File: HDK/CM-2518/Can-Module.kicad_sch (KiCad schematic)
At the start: 13 parts, among them J101 Can Connect, J102 Can Connect, SW101 SW_DIP_x01, U101 SN65HVD230, U102 MCP2515-xST, Y101 8MHz

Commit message: added fd module
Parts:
- removed R102: 10K, Resistor_SMD:R_0402_1005Metric, symbol Device:R
- removed U102: MCP2515-xST, Package_SO:TSSOP-20_4.4x6.5mm_P0.65mm, symbol Interface_CAN_LIN:MCP2515-xST
- added U102: MCP2518FD, Package_SO:SOIC-14_3.9x8.7mm_P1.27mm, symbol Interface_CAN_LIN:MCP2517FD-xSL
- SW101: footprint Button_Switch_SMD:SW_DIP_SPSTx01_Slide_6.7x4.1mm_W6.73mm_P2.54mm_LowProfile_JPin -> Button_Switch_SMD:SW_DIP_SPSTx01_Slide_9.78x4.72mm_W8.61mm_P2.54mm
- Y101: value 8MHz -> 20MHz
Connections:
- net +3V3: now also U102.14 (VDD)
- net CAN_IRQ: now also U102.4 (~{INT})
- net CAN_RX: now also U102.2 (RXCAN)
- net CAN_TX: now also U102.1 (TXCAN)
- net GND: now also U102.7 (VSS)
- net OSC_IN: now also U102.6 (OSC1)
- net OSC_OUT: now also U102.5 (OSC2)
- net SOF: now also U102.3 (CLKO/SOF)
- net SPI_MISO: now also U102.12 (SDO)
- net SPI_MOSI: now also U102.11 (SDI)
- net SPI_SCK: now also U102.10 (SCK)
- net ~{CS}: now also U102.13 (nCS)
- no-connect marks 6 -> 3

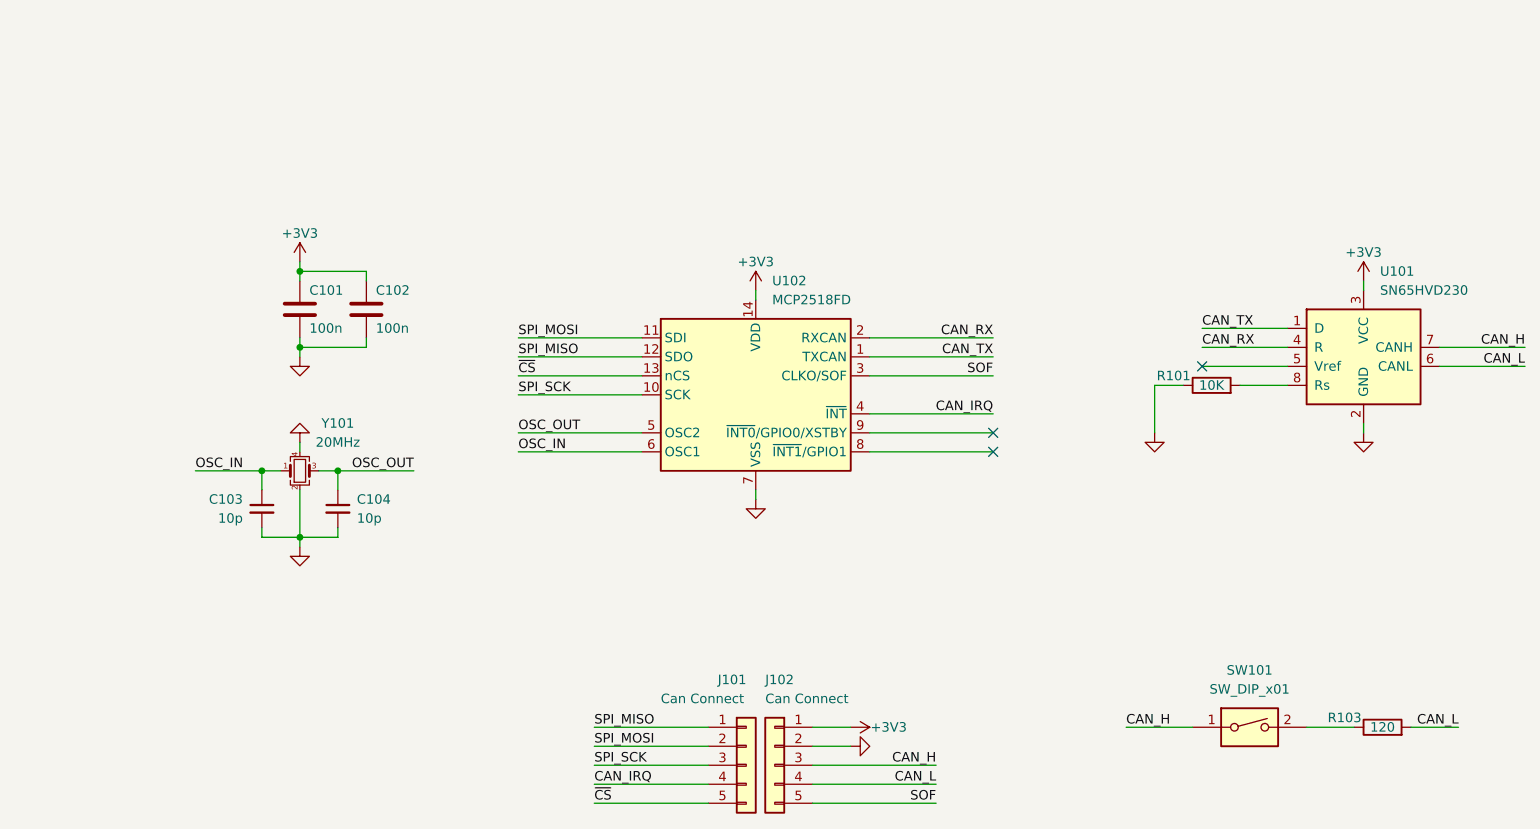
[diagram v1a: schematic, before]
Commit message: updated CM-2518FD Module
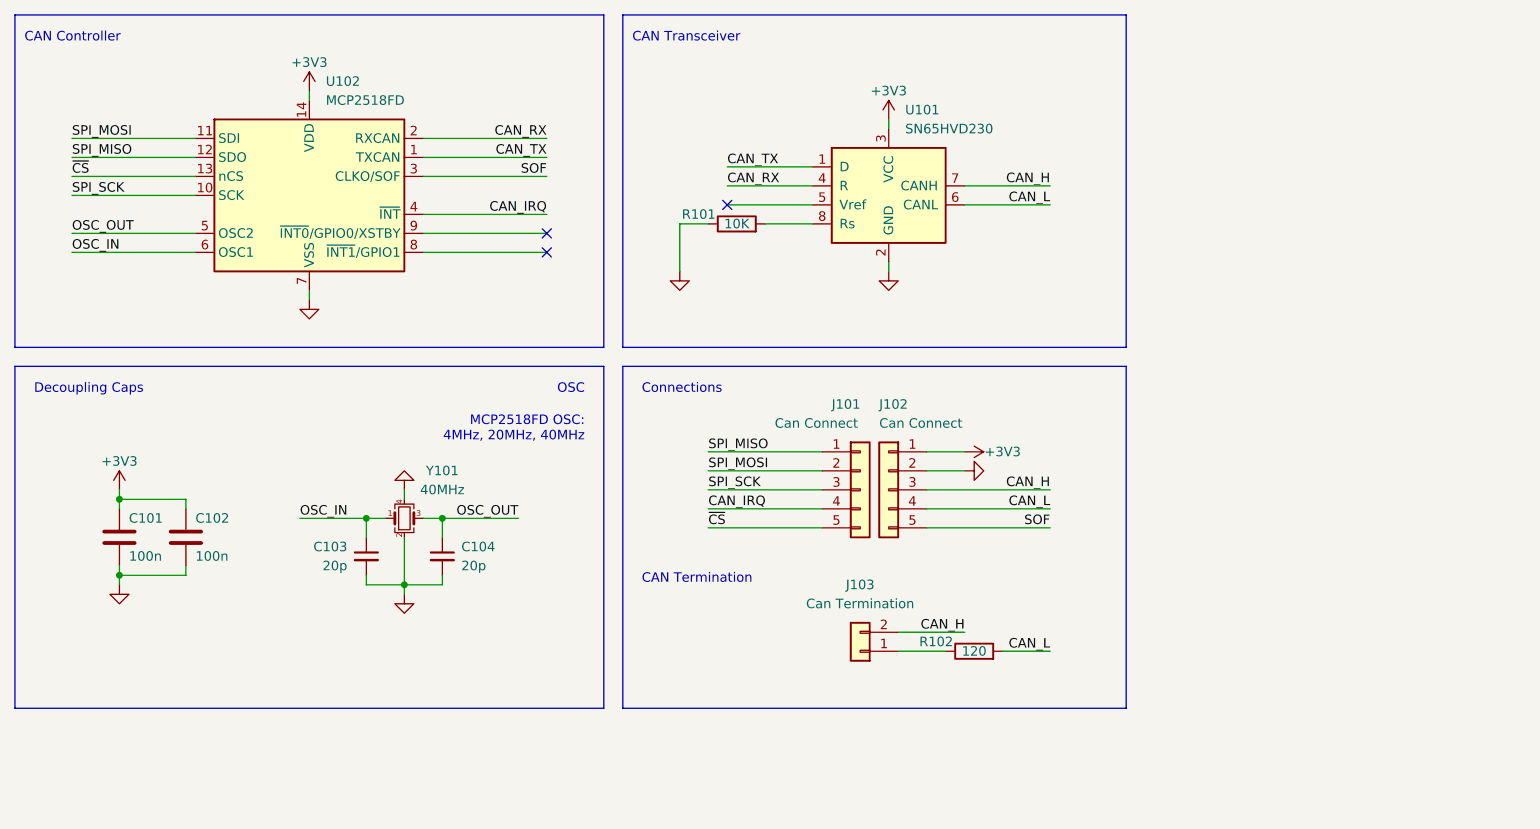
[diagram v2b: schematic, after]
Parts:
- removed SW101: SW_DIP_x01, Button_Switch_SMD:SW_DIP_SPSTx01_Slide_9.78x4.72mm_W8.61mm_P2.54mm, symbol Switch:SW_DIP_x01
- added J103: Can Termination, NVF-Kicad:PinHeader_1x02_P2.54mm_Horizontal, symbol Connector_Generic:Conn_01x02
- C101, C102: LCSC (none) -> C1523
- C103, C104: value 10p -> 20p; LCSC (none) -> C1554
- R101: LCSC (none) -> C25744
- R102: renamed from R103; footprint Resistor_SMD:R_0402_1005Metric -> Resistor_SMD:R_0805_2012Metric; LCSC (none) -> C17437
- U101: LCSC (none) -> C12084
- U102: LCSC (none) -> C626758
- Y101: value 20MHz -> 40MHz; LCSC (none) -> C9010
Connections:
- net CAN_H: now also J103.2 (Pin_2)
- net at R102.1: now also J103.1 (Pin_1)
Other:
- note added: "CAN Controller"
- note added: "CAN Termination"
- note added: "CAN Transceiver"
- note added: "Connections"
- note added: "Decoupling Caps"
- note added: "MCP2518FD OSC: 4MHz, 20MHz, 40MHz"
- note added: "OSC"
- company: (none) -> Scott CJX
- title: (none) -> Can Bus Module MCP2518FD
- moved on the sheet: C101, C102, C103, C104, J101, J102, R101, R102, U101, U102, Y101

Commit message: updated can-module
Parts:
- removed J101, J102: Can Connect, Connector_PinHeader_2.54mm:PinHeader_1x05_P2.54mm_Vertical, symbol Connector_Generic:Conn_01x05
- added J101: MCP251X, NVF-Kicad:Can-Module-CM251X, symbol NVF-Kicad:CM251X
- renumbered J103 to J102, U102 to U101, U101 to U102
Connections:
- net +3V3: now also J101.10 (GND)
- net CAN_H: now also J101.8 (CAN_H)
- net CAN_IRQ: now also J101.2 (CAN_IRQ)
- net CAN_L: now also J101.7 (CAN_L)
- net GND: now also J101.9 (VCC)
- net SOF: now also J101.6 (SOF)
- net SPI_MISO: now also J101.5 (MISO)
- net SPI_MOSI: now also J101.4 (MOSI)
- net SPI_SCK: now also J101.3 (SCK)
- net ~{CS}: now also J101.1 (~{CS})
